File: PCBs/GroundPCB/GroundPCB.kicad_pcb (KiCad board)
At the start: 4 copper layers, 85 x 100 mm, 41 parts, among them IC1 SWITCH-HSWA4-63DR+, IC2 SWITCH-HSWA4-63DR+, J1 SMA-LPRS-CONNECTOR, U1 HMC452ST89ETR, U2 PGA-103+, U3 RFM96W-433S2, U4 DS3231M

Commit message: initial layout changes
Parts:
- added H1: MountingHole, MountingHole:MountingHole_2.5mm, F.Cu at (103.5, 57.0)
- added H2: MountingHole, MountingHole:MountingHole_2.5mm, F.Cu at (181.5, 57.0)
- added H3: MountingHole, MountingHole:MountingHole_2.5mm, F.Cu at (181.5, 150.0)
- added H4: MountingHole, MountingHole:MountingHole_2.5mm, F.Cu at (103.5, 150.0)
- added J2: Conn_01x04, Connector_JST:JST_SH_SM04B-SRSS-TB_1x04-1MP_P1.00mm_Horizontal, F.Cu at (152.5, 57.5)
- added J3: Conn_01x04, Connector_JST:JST_SH_SM04B-SRSS-TB_1x04-1MP_P1.00mm_Horizontal, F.Cu at (162.5, 57.5)
- added SW1: SW_SPST, Button_Switch_THT:SW_Push_2P1T_Toggle_CK_PVA1xxH1xxxxxxV2, F.Cu at (47.6, 115.6)
- added TP1: , TestPoint:TestPoint_Pad_D2.0mm, F.Cu at (84.0, 90.1)
- added TP10: , TestPoint:TestPoint_Pad_D2.0mm, F.Cu at (88.0, 86.1)
- added TP11: , TestPoint:TestPoint_Pad_D2.0mm, F.Cu at (84.0, 86.1)
- added TP12: , TestPoint:TestPoint_Pad_D2.0mm, F.Cu at (88.0, 90.1)
- added TP13: , TestPoint:TestPoint_Pad_D2.0mm, F.Cu at (63.8, 104.6)
- added TP14: , TestPoint:TestPoint_Pad_D2.0mm, F.Cu at (71.9, 105.1)
- added TP15: , TestPoint:TestPoint_Pad_D2.0mm, F.Cu at (81.3, 94.2)
- added TP16: , TestPoint:TestPoint_Pad_D2.0mm, F.Cu at (59.8, 104.6)
- added TP17: , TestPoint:TestPoint_Pad_D2.0mm, F.Cu at (67.9, 104.6)
- added TP18: , TestPoint:TestPoint_Pad_D2.0mm, F.Cu at (79.9, 90.1)
- added TP19: , TestPoint:TestPoint_Pad_D2.0mm, F.Cu at (79.9, 86.1)
- added TP2: , TestPoint:TestPoint_Pad_D2.0mm, F.Cu at (75.8, 86.1)
- added TP3: , TestPoint:TestPoint_Pad_D2.0mm, F.Cu at (51.7, 102.6)
- added TP4: , TestPoint:TestPoint_Pad_D2.0mm, F.Cu at (73.2, 97.0)
- added TP5: , TestPoint:TestPoint_Pad_D2.0mm, F.Cu at (73.2, 101.0)
- added TP6: , TestPoint:TestPoint_Pad_D2.0mm, F.Cu at (55.7, 102.6)
- added TP7: , TestPoint:TestPoint_Pad_D2.0mm, F.Cu at (75.8, 90.1)
- added TP8: , TestPoint:TestPoint_Pad_D2.0mm, F.Cu at (77.2, 94.2)
- added TP9: , TestPoint:TestPoint_Pad_D2.0mm, F.Cu at (77.2, 98.2)
- BT1: moved to B.Cu
- moved BT1 29.0 mm to (128.0, 65.0)
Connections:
- A1 pad 1: unconnected-(A1-Pad1) -> +3.3V
- A1 pad 24: CS -> unconnected-(A1-Pad24)
- A1 pad 26: unconnected-(A1-Pad26) -> CS
- A1 pad 36: unconnected-(A1-Pad36) -> BUT1
- A1 pad 38: unconnected-(A1-Pad38) -> BUT2
- A1 pad 40: unconnected-(A1-Pad40) -> BUT3
- C8 pad 1: +5V -> Net-(C8-Pad1)
- C9 pad 1: +5V -> Net-(C8-Pad1)
- L5 pad 1: +5V -> Net-(C8-Pad1)
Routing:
- net +3.3V: track 56.3 -> 91.3 mm
- net BUT1: track 0.00 -> 21.6 mm
- net BUT2: track 0.00 -> 21.0 mm
- net BUT3: track 0.00 -> 20.4 mm
- net SCL: track 42.2 -> 60.1 mm
- net SDA: track 51.4 -> 65.9 mm
- net Net-(BT1-PadP): track 17.1 -> 4.89 mm, vias 0 -> 1
- net Net-(C8-Pad1): track 0.00 -> 9.18 mm, vias 0 -> 1
- net +5V: track 53.7 -> 44.5 mm, vias 7 -> 6

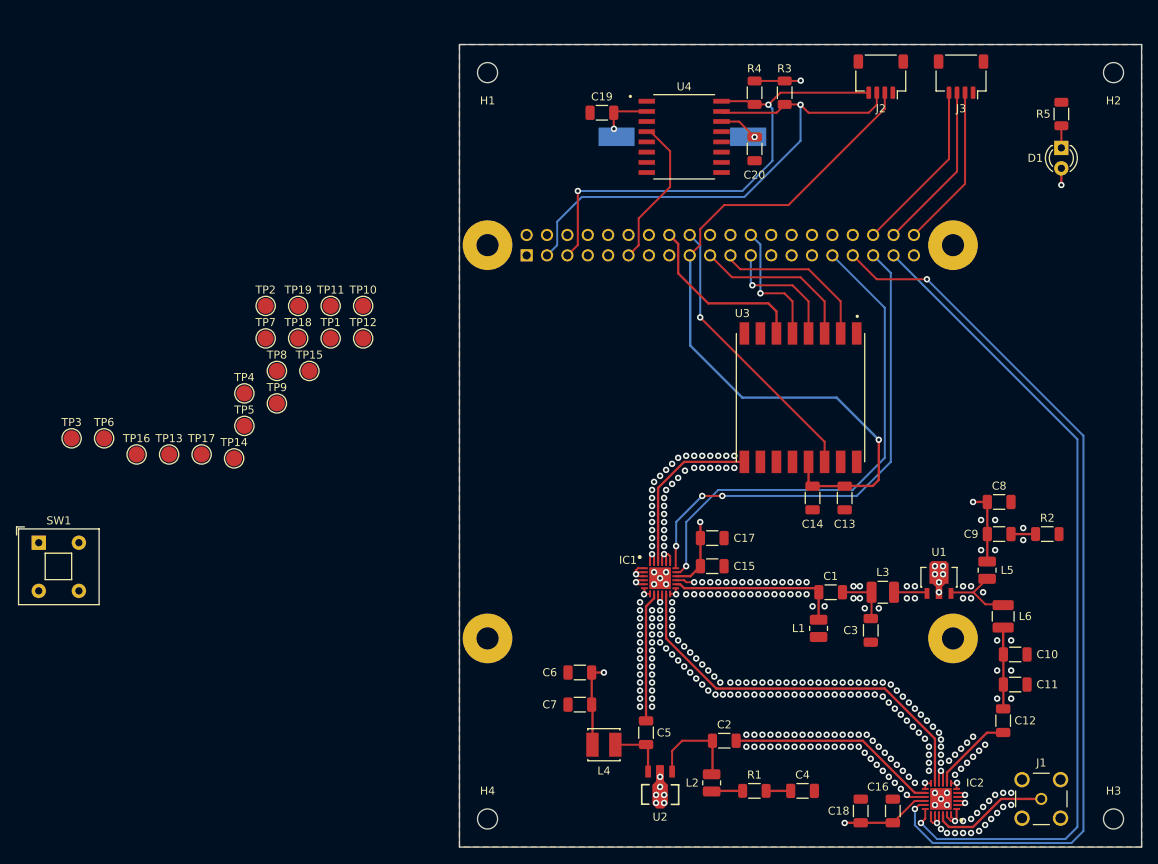
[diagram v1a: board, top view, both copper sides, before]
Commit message: relocated components, added switch to layout
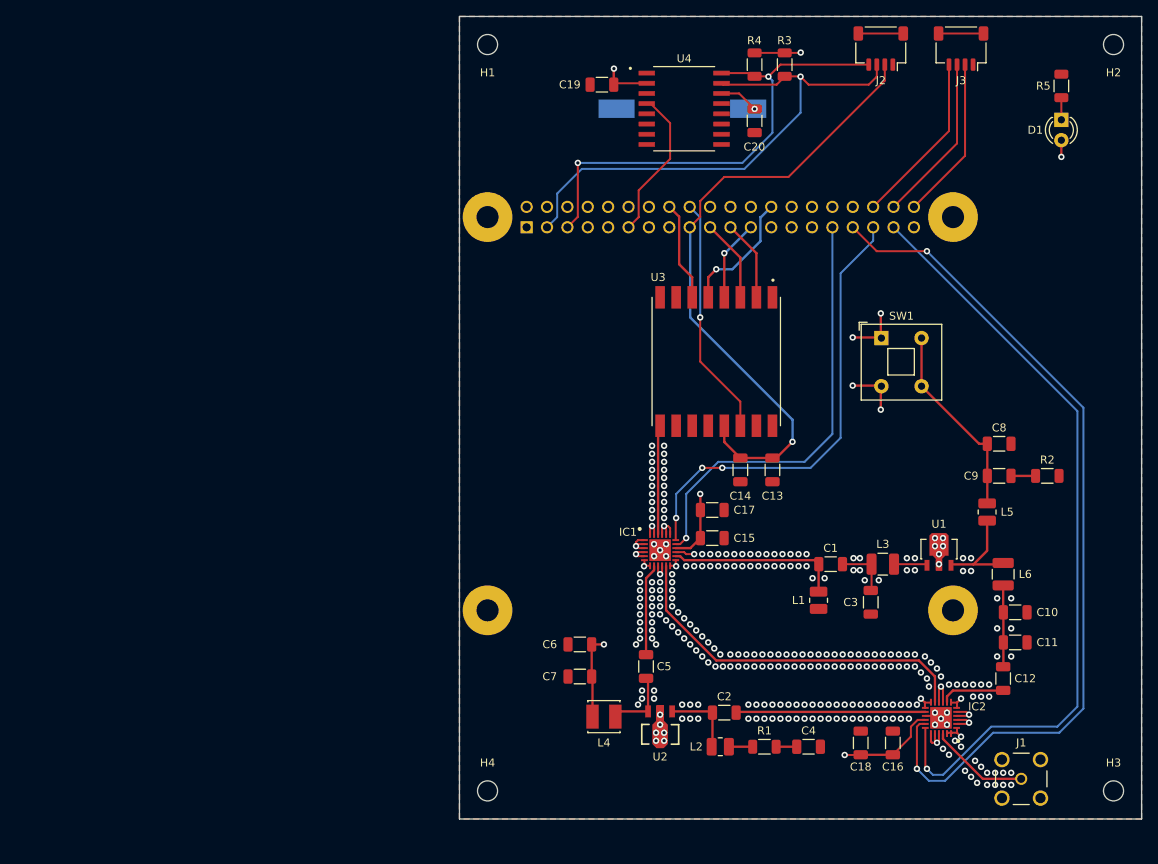
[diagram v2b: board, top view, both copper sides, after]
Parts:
- removed TP1, TP10, TP11, TP12, TP13, TP14, TP15, TP16, TP17, TP18, TP19, TP2, TP3, TP4, TP5, TP6, TP7, TP8, TP9: , TestPoint:TestPoint_Pad_D2.0mm
- moved SW1 108.1 mm to (152.6, 90.1)
- moved U3 11.4 mm to (132.0, 93.0)
- moved IC2 10.1 mm to (160.0, 137.5)
- moved C13 9.66 mm to (139.0, 106.5)
- moved C14 9.66 mm to (135.0, 106.5)
- moved C16 8.47 mm to (154.0, 140.5)
- moved C18 8.47 mm to (150.0, 140.5)
- moved C5 8.25 mm to (123.2, 131.0)
- moved U2 7.50 mm to (125.0, 138.5)
- moved C8 7.25 mm to (167.2, 103.2)
- moved C9 7.25 mm to (167.2, 107.2)
- moved L5 7.25 mm to (165.8, 111.8)
- moved R2 7.25 mm to (173.2, 107.2)
- moved R1 5.64 mm to (138.0, 141.0)
- moved C4 5.55 mm to (143.5, 141.0)
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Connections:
- A1 pad 1: +3.3V -> unconnected-(A1-Pad1)
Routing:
- net Net-(C8-Pad1): track 9.18 -> 24.6 mm, vias 1 -> 0
- net +5V: track 44.5 -> 58.7 mm, vias 6 -> 10
- net +3.3V: track 91.3 -> 78.7 mm
- net MOSI: track 20.6 -> 10.3 mm
- net MISO: track 19.9 -> 10.1 mm
- net RST-TRX: track 22.2 -> 12.5 mm
- net CTRL1A: track 63.1 -> 54.2 mm
- net TRX: track 21.4 -> 13.3 mm
- net CTRL2B: track 103.6 -> 97.0 mm
- net CTRL1B: track 113.4 -> 107.1 mm
- net unconnected-(J3-PadMP): track 0.00 -> 5.60 mm
- net unconnected-(J2-PadMP): track 0.00 -> 5.60 mm
- net SCLK: track 15.6 -> 10.1 mm
- net DIO0: track 35.2 -> 29.9 mm
- net CTRL2A: track 62.3 -> 57.1 mm
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
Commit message: post-review revisions
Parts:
- C13: value 10u -> 1u
- C14: value 0.1u -> 100n
- C15, C16: value 100p -> 100n
- C19, C20: value 0.47u -> 100n
- C2, C5: value 0.01u -> 10n
- C7: value 0.33u -> 330n
- moved C13 25.6 mm to (114.5, 99.0)
- moved C14 17.7 mm to (119.0, 99.0)
- moved R2 13.5 mm to (160.0, 104.5), turned to 180 degrees
- moved C4 8.84 mm to (144.8, 132.2)
- moved R1 8.76 mm to (138.5, 132.2)
- moved L2 8.75 mm to (132.6, 132.2)
- moved U1 4.01 mm to (160.0, 112.5)
- moved C1 4.00 mm to (146.2, 114.2)
- moved C15 4.00 mm to (131.5, 111.0)
- moved C17 4.00 mm to (131.5, 107.5)
- moved C3 4.00 mm to (151.2, 119.0)
- moved IC1 4.00 mm to (125.0, 112.4)
- moved L1 4.00 mm to (144.8, 118.8)
- moved L3 4.00 mm to (152.8, 114.2)
- moved C12 3.82 mm to (164.0, 131.8), turned to 180 degrees
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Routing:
- net +5V: track 58.7 -> 46.9 mm, vias 10 -> 7
- net CTRL1B: track 107.1 -> 100.7 mm
- net CTRL2B: track 97.0 -> 91.0 mm
- net Net-(BT1-PadP): track 4.89 -> 9.25 mm
- net TRX: track 13.3 -> 9.30 mm
- net LNA-TRX: track 11.5 -> 15.5 mm
- net NOAMP: track 45.7 -> 49.5 mm
- net Net-(C8-Pad1): track 24.6 -> 27.9 mm
- net PAMP-ANT: track 8.00 -> 4.89 mm
- net Net-(C10-Pad1): track 10.1 -> 13.0 mm
- net CTRL2A: track 57.1 -> 54.8 mm, vias 3 -> 1
- net GND: track 43.7 -> 45.3 mm, vias 291 -> 299
- net +3.3V: track 78.7 -> 77.5 mm, vias 1 -> 2
- net Net-(IC2-Pad22): track 12.5 -> 13.5 mm
- net Net-(C5-Pad1): track 8.22 -> 7.29 mm
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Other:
- board text added: "Adam S, Carter J, Elaine R, Emily M, Henry P, Jonathan A, Maya B, Mitchell H, Rosemary L"
- board text added: "NARWAL"
- board text added: "Rice Eclipse"
- board text added: "v1"
